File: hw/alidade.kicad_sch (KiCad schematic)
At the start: 0 parts

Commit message: Battery Monitor
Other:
- sheet Power ports: added BATMON, BATMONEN, rBATMON, rBATMONEN; removed none
- sheet Processor ports: added BATMON, BATMONEN, rBATMON, rBATMONEN; removed none
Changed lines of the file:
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@@
+	(wire
+		(pts
+			(xy 105.41 187.96) (xy 123.19 187.96)
+		)
+		(stroke
+			(width 0)
+			(type default)
+		)
+	)
+	(wire
+		(pts
+			(xy 105.41 167.64) (xy 123.19 167.64)
+		)
+		(stroke
+			(width 0)
+			(type default)
+		)
+	)
 	(wire
 		(pts
@@
 	(wire
 		(pts
-			(xy 105.41 171.45) (xy 123.19 171.45)
+			(xy 105.41 195.58) (xy 123.19 195.58)
+		)
+		(stroke
+			(width 0)
+			(type default)
+		)
+	)
+	(wire
+		(pts
+			(xy 105.41 180.34) (xy 123.19 180.34)
+		)
+		(stroke
+			(width 0)
+			(type default)
+		)
+	)
+	(wire
+		(pts
+			(xy 105.41 177.8) (xy 123.19 177.8)
 		)
 		(stroke
@@
 	(wire
 		(pts
-			(xy 105.41 181.61) (xy 123.19 181.61)
+			(xy 105.41 170.18) (xy 123.19 170.18)
 		)
 		(stroke
@@
 	(wire
 		(pts
-			(xy 105.41 173.99) (xy 123.19 173.99)
-		)
-		(stroke
-			(width 0)
-			(type default)
-		)
-	)
-	(wire
-		(pts
-			(xy 105.41 195.58) (xy 123.19 195.58)
-		)
-		(stroke
-			(width 0)
-			(type default)
-		)
-	)
-	(wire
-		(pts
-			(xy 105.41 179.07) (xy 123.19 179.07)
-		)
-		(stroke
-			(width 0)
-			(type default)
-		)
-	)
-	(wire
-		(pts
-			(xy 105.41 176.53) (xy 123.19 176.53)
+			(xy 105.41 190.5) (xy 123.19 190.5)
+		)
+		(stroke
+			(width 0)
+			(type default)
+		)
+	)
+	(wire
+		(pts
+			(xy 105.41 175.26) (xy 123.19 175.26)
+		)
+		(stroke
+			(width 0)
+			(type default)
+		)
+	)
+	(wire
+		(pts
+			(xy 105.41 172.72) (xy 123.19 172.72)
+		)
+		(stroke
+			(width 0)
+			(type default)
+		)
+	)
+	(wire
+		(pts
+			(xy 105.41 182.88) (xy 123.19 182.88)
 		)
 		(stroke
@@
 	)
 	(sheet
-		(at 90.17 168.91)
-		(size 15.24 36.83)
+		(at 81.28 165.1)
+		(size 24.13 40.64)
 		(exclude_from_sim no)
 		(in_bom yes)
@@
 		)
 		(property "Sheetname" "Power"
-			(at 90.17 168.1984 0)
+			(at 81.28 164.3884 0)
 			(effects
 				(font
@@
 		)
 		(property "Sheetfile" "power.kicad_sch"
-			(at 90.17 206.3246 0)
+			(at 81.28 206.3246 0)
 			(effects
 				(font
@@
 		)
 		(pin "ISET" input
-			(at 105.41 176.53 0)
+			(at 105.41 172.72 0)
 			(effects
 				(font
@@
 		)
 		(pin "MODE" input
-			(at 105.41 179.07 0)
+			(at 105.41 175.26 0)
 			(effects
 				(font
@@
 		)
 		(pin "rISET" input
+			(at 105.41 193.04 0)
+			(effects
+				(font
+					(size 1.27 1.27)
+				)
+				(justify right)
+			)
+		)
+		(pin "rMODE" input
+			(at 105.41 195.58 0)
+			(effects
+				(font
+					(size 1.27 1.27)
+				)
+				(justify right)
+			)
+		)
+		(pin "rSHPACT" input
 			(at 105.41 198.12 0)
 			(effects
@@
 			)
 		)
-		(pin "rMODE" input
+		(pin "SHPACT" input
+			(at 105.41 177.8 0)
+			(effects
+				(font
+					(size 1.27 1.27)
+				)
+				(justify right)
+			)
+		)
+		(pin "rSHPHLD" input
+			(at 81.28 189.23 180)
+			(effects
+				(font
+					(size 1.27 1.27)
+				)
+				(justify left)
+			)
+		)
+		(pin "SHPHLD" input
+			(at 81.28 185.42 180)
+			(effects
+				(font
+					(size 1.27 1.27)
+				)
+				(justify left)
+			)
+		)
+		(pin "CHG" output
+			(at 105.41 167.64 0)
+			(effects
+				(font
+					(size 1.27 1.27)
+				)
+				(justify right)
+			)
+		)
+		(pin "ERR" output
+			(at 105.41 170.18 0)
+			(effects
+				(font
+					(size 1.27 1.27)
+				)
+				(justify right)
+			)
+		)
+		(pin "rCHG" output
+			(at 105.41 187.96 0)
+			(effects
+				(font
+					(size 1.27 1.27)
+				)
+				(justify right)
+			)
+		)
+		(pin "rERR" output
+			(at 105.41 190.5 0)
+			(effects
+				(font
+					(size 1.27 1.27)
+				)
+				(justify right)
+			)
+		)
+		(pin "BATMON" output
+			(at 105.41 180.34 0)
+			(effects
+				(font
+					(size 1.27 1.27)
+				)
+				(justify right)
+			)
+		)
+		(pin "BATMONEN" input
+			(at 105.41 182.88 0)
+			(effects
+				(font
+					(size 1.27 1.27)
+				)
+				(justify right)
+			)
+		)
+		(pin "rBATMON" output
 			(at 105.41 200.66 0)
 			(effects
@@
 			)
 		)
-		(pin "rSHPACT" input
+		(pin "rBATMONEN" input
 			(at 105.41 203.2 0)
-			(effects
-				(font
-					(size 1.27 1.27)
-				)
-				(justify right)
-			)
-		)
-		(pin "SHPACT" input
-			(at 105.41 181.61 0)
-			(effects
-				(font
-					(size 1.27 1.27)
-				)
-				(justify right)
-			)
-		)
-		(pin "rSHPHLD" input
-			(at 90.17 189.23 180)
-			(effects
-				(font
-					(size 1.27 1.27)
-				)
-				(justify left)
-			)
-		)
-		(pin "SHPHLD" input
-			(at 90.17 185.42 180)
-			(effects
-				(font
-					(size 1.27 1.27)
-				)
-				(justify left)
-			)
-		)
-		(pin "CHG" output
-			(at 105.41 171.45 0)
-			(effects
-				(font
-					(size 1.27 1.27)
-				)
-				(justify right)
-			)
-		)
-		(pin "ERR" output
-			(at 105.41 173.99 0)
-			(effects
-				(font
-					(size 1.27 1.27)
-				)
-				(justify right)
-			)
-		)
-		(pin "rCHG" output
-			(at 105.41 193.04 0)
-			(effects
-				(font
-					(size 1.27 1.27)
-				)
-				(justify right)
-			)
-		)
-		(pin "rERR" output
-			(at 105.41 195.58 0)
 			(effects
 				(font
@@
 		)
 		(pin "CHG" input
-			(at 123.19 171.45 180)
+			(at 123.19 167.64 180)
 			(effects
 				(font
@@
 		)
 		(pin "ERR" input
-			(at 123.19 173.99 180)
+			(at 123.19 170.18 180)
 			(effects
 				(font
@@
 		)
 		(pin "rCHG" input
+			(at 123.19 187.96 180)
+			(effects
+				(font
+					(size 1.27 1.27)
+				)
+				(justify left)
+			)
+		)
+		(pin "rERR" input
+			(at 123.19 190.5 180)
+			(effects
+				(font
+					(size 1.27 1.27)
+				)
+				(justify left)
+			)
+		)
+		(pin "ISET" output
+			(at 123.19 172.72 180)
+			(effects
+				(font
+					(size 1.27 1.27)
+				)
+				(justify left)
+			)
+		)
+		(pin "MODE" output
+			(at 123.19 175.26 180)
+			(effects
+				(font
+					(size 1.27 1.27)
+				)
+				(justify left)
+			)
+		)
+		(pin "SHPACT" output
+			(at 123.19 177.8 180)
+			(effects
+				(font
+					(size 1.27 1.27)
+				)
+				(justify left)
+			)
+		)
+		(pin "rISET" output
 			(at 123.19 193.04 180)
 			(effects
@@
 			)
 		)
-		(pin "rERR" input
+		(pin "rMODE" output
 			(at 123.19 195.58 180)
 			(effects
@@
 			)
 		)
-		(pin "ISET" output
-			(at 123.19 176.53 180)
-			(effects
-				(font
-					(size 1.27 1.27)
-				)
-				(justify left)
-			)
-		)
-		(pin "MODE" output
-			(at 123.19 179.07 180)
-			(effects
-				(font
-					(size 1.27 1.27)
-				)
-				(justify left)
-			)
-		)
-		(pin "SHPACT" output
-			(at 123.19 181.61 180)
-			(effects
-				(font
-					(size 1.27 1.27)
-				)
-				(justify left)
-			)
-		)
-		(pin "rISET" output
+		(pin "rSHPACT" output
 			(at 123.19 198.12 180)
 			(effects
@@
 			)
 		)
-		(pin "rMODE" output
+		(pin "BATMON" input
+			(at 123.19 180.34 180)
+			(effects
+				(font
+					(size 1.27 1.27)
+				)
+				(justify left)
+			)
+		)
+		(pin "BATMONEN" output
+			(at 123.19 182.88 180)
+			(effects
+				(font
+					(size 1.27 1.27)
+				)
+				(justify left)
+			)
+		)
+		(pin "rBATMON" input
 			(at 123.19 200.66 180)
 			(effects
@@
 			)
 		)
-		(pin "rSHPACT" output
+		(pin "rBATMONEN" output
 			(at 123.19 203.2 180)
 			(effects

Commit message: Switch matrix and sheet pins
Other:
- sheet Processor ports: added COL0, COL1, COL2, COL3, COL4, COL5, COL6, ROW0, ROW1, ROW2, ROW3, rCOL0, rCOL1, rCOL2, rCOL3, rCOL4, rCOL5, rCOL6, rROW0, rROW1, rROW2, rROW3; removed none
- sheet Switches ports: added COL0, COL1, COL2, COL3, COL4, COL5, COL6, ROW0, ROW1, ROW2, ROW3, rCOL0, rCOL1, rCOL2, rCOL3, rCOL4, rCOL5, rCOL6, rROW0, rROW1, rROW2, rROW3; removed none

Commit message: Sheet pins
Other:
- sheet Power ports: added PMICINT, SCL, SDA, rPMICINT, rSCL, rSDA; removed BATMON, BATMONEN, CHG, ERR, ISET, MODE, SHPACT, rBATMON, rBATMONEN, rCHG, rERR, rISET, rMODE, rSHPACT
- sheet Processor ports: added PMICINT, SCL, SDA, rPMICINT, rSCL, rSDA; removed BATMON, BATMONEN, CHG, ERR, ISET, MODE, SHPACT, rBATMON, rBATMONEN, rCHG, rERR, rISET, rMODE, rSHPACT

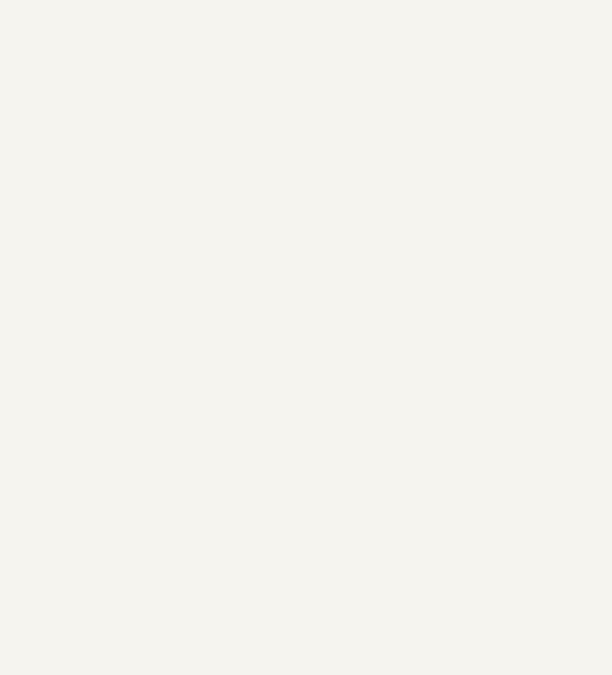
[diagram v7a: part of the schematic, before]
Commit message: Decoder symbol
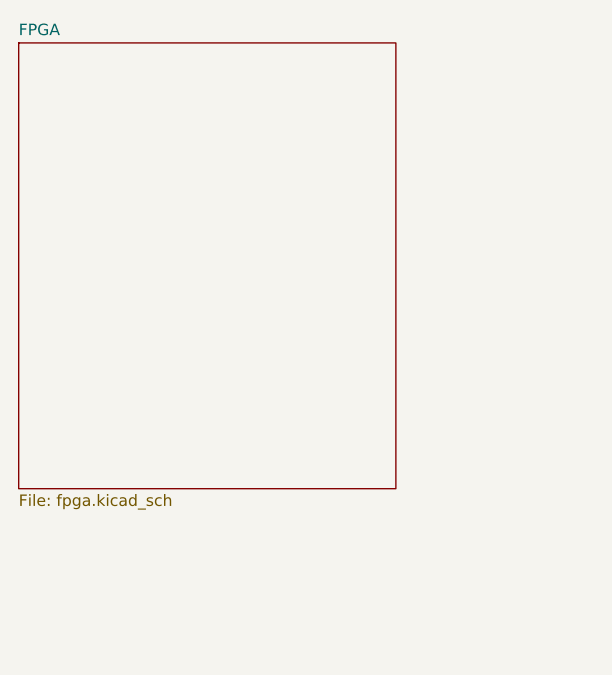
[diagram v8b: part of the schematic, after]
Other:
- added sheet FPGA (fpga.kicad_sch)
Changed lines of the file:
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@@
+		)
+	)
+	(sheet
+		(at 39.37 64.77)
+		(size 41.91 49.53)
+		(exclude_from_sim no)
+		(in_bom yes)
+		(on_board yes)
+		(dnp no)
+		(fields_autoplaced yes)
+		(stroke
+			(width 0.1524)
+			(type solid)
+		)
+		(fill
+			(color 0 0 0 0.0000)
+		)
+		(property "Sheetname" "FPGA"
+			(at 39.37 64.0584 0)
+			(effects
+				(font
+					(size 1.27 1.27)
+				)
+				(justify left bottom)
+			)
+		)
+		(property "Sheetfile" "fpga.kicad_sch"
+			(at 39.37 114.8846 0)
+			(effects
+				(font
+					(size 1.27 1.27)
+				)
+				(justify left top)
+			)
+		)
+		(instances
+			(project "alidade"
+				(path "/4cc5d416-57f5-4147-8183-e03ae6b1198a"
+					(page "5")
+				)
+			)
 		)
 	)
